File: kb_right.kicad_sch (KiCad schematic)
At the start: 175 parts, among them J1 10029449-001RLF, J2 Conn_01x03, J3 Conn_01x06, J4 Conn_01x08, J5 Conn_01x09, SW0 RotaryEncoder_Switch

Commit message: added 1.75u right shift
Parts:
- added D32: D_Small, Diode_SMD:D_SOD-123, symbol Device:D_Small
- added MX32: MX-NoLED, MX_Only:MXOnly-2.75U-Hotswap-ReversedStabilizers, symbol MX_Alps_Hybrid:MX-NoLED
- added MX32_1: MX-NoLED, MX_Only:MXOnly-1.75U-Hotswap, symbol MX_Alps_Hybrid:MX-NoLED
- MX32_2: renamed from MX32; footprint MX_Only:MXOnly-2.75U-Hotswap -> MX_Only:MXOnly-1U-Hotswap
- renumbered D32 to D32_1
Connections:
- net COL5: now also MX32.1 (COL), MX32_1.1 (COL)
- net COL6: now also J5.2 (Pin_2); no longer J5.1 (Pin_1)
- net COL7: now also J5.8 (Pin_8); no longer J5.7 (Pin_7)
- net COL8: now also J5.9 (Pin_9); no longer J5.8 (Pin_8)
- net GND: now also J5.1 (Pin_1); no longer J5.9 (Pin_9)
- net ROW5: now also J5.3 (Pin_3); no longer J5.2 (Pin_2)
- net ROW6: now also J5.4 (Pin_4); no longer J5.3 (Pin_3)
- net ROW7: now also J5.5 (Pin_5); no longer J5.4 (Pin_4)
- net ROW8: now also J5.6 (Pin_6), D32.1 (K); no longer J5.5 (Pin_5)
- net ROW9: now also J5.7 (Pin_7); no longer J5.6 (Pin_6)
- new net: D32.2 (A), MX32.2 (ROW), MX32_1.2 (ROW)

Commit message: fixed split right shift
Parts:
- MX32: footprint MX_Only:MXOnly-2.75U-Hotswap-ReversedStabilizers -> MX_Only:MXOnly-2.75U-Hotswap
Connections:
- net COL6: now also J5.1 (Pin_1); no longer J5.2 (Pin_2)
- net COL7: now also J5.7 (Pin_7); no longer J5.8 (Pin_8)
- net COL8: now also J5.8 (Pin_8); no longer J5.9 (Pin_9)
- net GND: now also J5.9 (Pin_9); no longer J5.1 (Pin_1)
- net ROW5: now also J5.2 (Pin_2); no longer J5.3 (Pin_3)
- net ROW6: now also J5.3 (Pin_3); no longer J5.4 (Pin_4)
- net ROW7: now also J5.4 (Pin_4); no longer J5.5 (Pin_5)
- net ROW8: now also J5.5 (Pin_5); no longer J5.6 (Pin_6)
- net ROW9: now also J5.6 (Pin_6); no longer J5.7 (Pin_7)
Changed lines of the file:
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@@
     (stroke (width 0) (type default) (color 0 0 0 0))
   )
-  (wire (pts (xy 375.92 130.81) (xy 384.81 130.81))
-    (stroke (width 0) (type default) (color 0 0 0 0))
-  )
   (wire (pts (xy 132.08 46.99) (xy 132.08 52.07))
     (stroke (width 0) (type default) (color 0 0 0 0))
@@
     (stroke (width 0) (type default) (color 0 0 0 0))
   )
+  (label "COL7" (at 384.81 146.05 180)
+    (effects (font (size 1.27 1.27)) (justify right bottom))
+  )
   (label "COL4" (at 180.34 24.13 90)
     (effects (font (size 1.27 1.27)) (justify left bottom))
   )
+  (label "ROW8" (at 384.81 140.97 180)
+    (effects (font (size 1.27 1.27)) (justify right bottom))
+  )
   (label "COL0" (at 396.24 31.75 0)
     (effects (font (size 1.27 1.27)) (justify left bottom))
   )
-  (label "ROW7" (at 384.81 140.97 180)
-    (effects (font (size 1.27 1.27)) (justify right bottom))
-  )
   (label "ROW8" (at 30.48 139.7 180)
     (effects (font (size 1.27 1.27)) (justify right bottom))
@@
     (effects (font (size 1.27 1.27)) (justify left bottom))
   )
+  (label "COL6" (at 384.81 130.81 180)
+    (effects (font (size 1.27 1.27)) (justify right bottom))
+  )
   (label "ROW9" (at 370.84 24.13 180)
     (effects (font (size 1.27 1.27)) (justify right bottom))
@@
     (effects (font (size 1.27 1.27)) (justify right bottom))
   )
-  (label "ROW8" (at 384.81 143.51 180)
-    (effects (font (size 1.27 1.27)) (justify right bottom))
-  )
   (label "RGB_IN" (at 370.84 46.99 180)
     (effects (font (size 1.27 1.27)) (justify right bottom))
@@
     (effects (font (size 1.27 1.27)) (justify left bottom))
   )
-  (label "ROW6" (at 384.81 138.43 180)
-    (effects (font (size 1.27 1.27)) (justify right bottom))
-  )
   (label "ROW7" (at 370.84 26.67 180)
     (effects (font (size 1.27 1.27)) (justify right bottom))
@@
     (effects (font (size 1.27 1.27)) (justify right bottom))
   )
-  (label "COL8" (at 384.81 151.13 180)
+  (label "ROW9" (at 384.81 143.51 180)
     (effects (font (size 1.27 1.27)) (justify right bottom))
   )
@@
     (effects (font (size 1.27 1.27)) (justify right bottom))
   )
-  (label "COL6" (at 384.81 133.35 180)
-    (effects (font (size 1.27 1.27)) (justify right bottom))
-  )
   (label "COL1" (at 97.79 24.13 90)
     (effects (font (size 1.27 1.27)) (justify left bottom))
@@
     (effects (font (size 1.27 1.27)) (justify right bottom))
   )
+  (label "ROW6" (at 384.81 135.89 180)
+    (effects (font (size 1.27 1.27)) (justify right bottom))
+  )
   (label "ENC_R1" (at 273.05 33.02 180)
     (effects (font (size 1.27 1.27)) (justify right bottom))
@@
     (effects (font (size 1.27 1.27)) (justify right bottom))
   )
-  (label "COL7" (at 384.81 148.59 180)
-    (effects (font (size 1.27 1.27)) (justify right bottom))
-  )
   (label "COL3" (at 370.84 34.29 180)
     (effects (font (size 1.27 1.27)) (justify right bottom))
@@
     (effects (font (size 1.27 1.27)) (justify right bottom))
   )
-  (label "ROW5" (at 384.81 135.89 180)
+  (label "COL8" (at 384.81 148.59 180)
     (effects (font (size 1.27 1.27)) (justify right bottom))
   )
@@
     (effects (font (size 1.27 1.27)) (justify left bottom))
   )
+  (label "ROW7" (at 384.81 138.43 180)
+    (effects (font (size 1.27 1.27)) (justify right bottom))
+  )
   (label "COL2" (at 396.24 34.29 0)
     (effects (font (size 1.27 1.27)) (justify left bottom))
@@
     (effects (font (size 1.27 1.27)) (justify left bottom))
   )
-  (label "ROW9" (at 384.81 146.05 180)
+  (label "ROW5" (at 384.81 133.35 180)
     (effects (font (size 1.27 1.27)) (justify right bottom))
   )
@@
     (pin "2")
   )
+  (symbol (lib_id "power:GND") (at 384.81 151.13 0) (unit 1)
+    (in_bom yes) (on_board yes) (fields_autoplaced)
+    (property "Reference" "#PWR?" (id 0) (at 384.81 157.48 0)
+      (effects (font (size 1.27 1.27)) hide)
+    )
+    (property "Value" "GND" (id 1) (at 384.81 156.21 0))
+    (property "Footprint" "" (id 2) (at 384.81 151.13 0)
+      (effects (font (size 1.27 1.27)) hide)
+    )
+    (property "Datasheet" "" (id 3) (at 384.81 151.13 0)
+      (effects (font (size 1.27 1.27)) hide)
+    )
+    (pin "1")
+  )
   (symbol (lib_id "power:GND") (at 255.27 262.89 0) (unit 1)
     (in_bom yes) (on_board yes) (fields_autoplaced)
@@
     (pin "2")
   )
-  (symbol (lib_id "power:GND") (at 375.92 130.81 0) (unit 1)
-    (in_bom yes) (on_board yes) (fields_autoplaced)
-    (property "Reference" "#PWR?" (id 0) (at 375.92 137.16 0)
-      (effects (font (size 1.27 1.27)) hide)
-    )
-    (property "Value" "GND" (id 1) (at 375.92 135.89 0))
-    (property "Footprint" "" (id 2) (at 375.92 130.81 0)
-      (effects (font (size 1.27 1.27)) hide)
-    )
-    (property "Datasheet" "" (id 3) (at 375.92 130.81 0)
-      (effects (font (size 1.27 1.27)) hide)
-    )
-    (pin "1")
-  )
   (symbol (lib_id "MX_Alps_Hybrid:MX-NoLED") (at 245.11 151.13 0) (unit 1)
     (in_bom yes) (on_board yes) (fields_autoplaced)
@@
       (effects (font (size 0.508 0.508)))
     )
-    (property "Footprint" "MX_Only:MXOnly-2.75U-Hotswap-ReversedStabilizers" (id 2) (at 182.245 122.555 0)
+    (property "Footprint" "MX_Only:MXOnly-2.75U-Hotswap" (id 2) (at 182.245 122.555 0)
       (effects (font (size 1.524 1.524)) hide)
     )
@@
       (reference "#PWR0187") (unit 1) (value "GND") (footprint "")
     )
-    (path "/7671b0de-2d92-498f-bb82-68e62219ea0b"
+    (path "/186d1e69-91a9-4165-a3fa-c15cfabc85a4"
       (reference "#PWR?") (unit 1) (value "GND") (footprint "")
     )
@@
     )
     (path "/bd5c7f90-342e-4ce2-8a8f-16d10e92a244"
-      (reference "MX32") (unit 1) (value "MX-NoLED") (footprint "MX_Only:MXOnly-2.75U-Hotswap-ReversedStabilizers")
+      (reference "MX32") (unit 1) (value "MX-NoLED") (footprint "MX_Only:MXOnly-2.75U-Hotswap")
     )
     (path "/b6c0f7f7-0224-4f0f-b9e7-b06cd4a6b8bd"

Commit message: start thru hole
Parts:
- added C?: 0.1uF, Capacitor_SMD:C_0805_2012Metric_Pad1.18x1.45mm_HandSolder, symbol Device:C_Small
- added D36: D_Small, Diode_SMD:D_SOD-123, symbol Device:D_Small
- added D?: SK6812MINI, Keebio-Parts:SK6812-MINI-E, symbol LED:WS2812B
- added MX36: MX-NoLED, MX_Only:MXOnly-1.25U-Hotswap, symbol MX_Alps_Hybrid:MX-NoLED
- added MX40_1: MX-NoLED, MX_Only:MXOnly-1.75U-Hotswap, symbol MX_Alps_Hybrid:MX-NoLED
- renumbered D36 to D37, D37 to D38, D38 to D39, D39 to D40, D40 to D41, D41 to D42, D42 to D43, MX36 to MX37, MX37 to MX38, MX38 to MX39, MX39 to MX40, MX40 to MX41, MX41 to MX42, MX42 to MX43
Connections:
- net +5V: now also C?.1, D?.1 (VDD)
- net COL0: now also J1.9; no longer J1.6
- net COL1: now also J1.8, MX36.1 (COL); no longer J1.7
- net COL2: now also J1.7; no longer J1.8
- net COL3: now also J1.6; no longer J1.9
- net COL4: now also J1.5; no longer J1.10
- net COL5: now also J1.4, MX40_1.1 (COL); no longer J1.11
- net COL6: now also J1.3; no longer J1.12
- net COL7: now also J1.2; no longer J1.13
- net COL8: now also J1.1; no longer J1.14
- net GND: now also C?.2, D?.3 (VSS)
- net ROW5: now also J1.10; no longer J1.5
- net ROW6: now also J1.11; no longer J1.4
- net ROW7: now also J1.12; no longer J1.3
- net ROW8: now also J1.13; no longer J1.2
- net ROW9: now also J1.14, D36.1 (K); no longer J1.1
- net at D142.2 (DOUT): now also D?.4 (DIN)
- net at D40.2 (A), MX40.2 (ROW): now also MX40_1.2 (ROW)
- new net: D36.2 (A), MX36.2 (ROW)

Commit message: try again - add rgb routing
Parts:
- removed C?: 0.1uF, Capacitor_SMD:C_0805_2012Metric_Pad1.18x1.45mm_HandSolder, symbol Device:C_Small
- removed D0, D43: D_Small, Diode_SMD:D_SOD-123, symbol Device:D_Small
- removed D?: SK6812MINI, Keebio-Parts:SK6812-MINI-E, symbol LED:WS2812B
- removed MX40_1: MX-NoLED, MX_Only:MXOnly-1.75U-Hotswap, symbol MX_Alps_Hybrid:MX-NoLED
- removed MX43: MX-NoLED, MX_Only:MXOnly-1U-Hotswap, symbol MX_Alps_Hybrid:MX-NoLED
- removed SW0: RotaryEncoder_Switch, Keebio-Parts:RotaryEncoder_EC11, symbol Device:RotaryEncoder_Switch
- added D45, D9: D_Small, Diode_SMD:D_SOD-123, symbol Device:D_Small
- added MX7_1: MX-NoLED, MX_Only:MXOnly-2U-Hotswap, symbol MX_Alps_Hybrid:MX-NoLED
- added MX9: MX-NoLED, MX_Only:MXOnly-1U-Hotswap, symbol MX_Alps_Hybrid:MX-NoLED
- added SW1: RotaryEncoder_Switch, Keebio-Parts:RotaryEncoder_EC11, symbol Device:RotaryEncoder_Switch
- MX41: renamed from MX40; footprint MX_Only:MXOnly-1.25U-Hotswap -> MX_Only:MXOnly-1U-Hotswap
- MX7: footprint MX_Only:MXOnly-2U-Hotswap -> MX_Only:MXOnly-1U-Hotswap
- renumbered D9 to D10, D10 to D11, D11 to D12, D12 to D13, D13 to D14, D14 to D15, D15 to D16, D16 to D17, D17 to D18, D18 to D19, D19 to D20, D20 to D21, D21 to D22, D22 to D23, D23 to D24, D24 to D25, D25 to D26, D26 to D27, D27 to D28, D28 to D29, D29 to D30, D30 to D31, D31 to D32, D32 to D35, D35 to D36, D36 to D37, D37 to D38, D38 to D39, D39 to D40, D40 to D41, D41 to D42, D42 to D43, MX9 to MX10, MX10 to MX11, MX11 to MX12, MX12 to MX13, MX13 to MX14, MX14 to MX15, MX15 to MX16, MX16 to MX17, MX17 to MX18, MX18 to MX19, MX19 to MX20, MX20 to MX21, MX21 to MX22, MX22 to MX23, MX23 to MX24, MX24 to MX25, MX25 to MX26, MX26 to MX27, MX27 to MX28, MX28 to MX29, MX29 to MX30, MX30 to MX31, MX31 to MX32, MX32_2 to MX32_1, MX32_1 to MX32_2, MX32 to MX33, MX33 to MX34, MX34 to MX35, MX35 to MX36, MX36 to MX37, MX37 to MX38, MX38 to MX39, MX39 to MX40, MX41 to MX42, MX42 to MX43
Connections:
- net COL6: now also MX7_1.1 (COL)
- net COL8: now also MX9.1 (COL), SW1.S1
- net ENC_R1: now also SW1.A
- net ENC_R2: now also SW1.B
- net GND: now also SW1.C
- net RGB_IN: now also D108.4 (DIN); no longer D101.4 (DIN)
- net ROW5: now also D9.1 (K)
- net ROW9: now also D45.1 (K)
- net at D106.2 (DOUT): now also D105.4 (DIN); no longer D107.4 (DIN)
- net at D106.4 (DIN): now also D107.2 (DOUT); no longer D105.2 (DOUT)
- net at D142.2 (DOUT): now also D141.4 (DIN)
- net at D142.4 (DIN): now also D134.2 (DOUT); no longer D141.2 (DOUT)
- net at D108.2 (DOUT): now also D107.4 (DIN); no longer D109.4 (DIN)
- net at D140.2 (DOUT): now also D139.4 (DIN); no longer D141.4 (DIN)
- net at D121.2 (DOUT): now also D120.4 (DIN); no longer D122.4 (DIN)
- net at D121.4 (DIN): now also D122.2 (DOUT); no longer D120.2 (DOUT)
- net at D104.2 (DOUT): now also D103.4 (DIN); no longer D105.4 (DIN)
- net at D104.4 (DIN): now also D105.2 (DOUT); no longer D103.2 (DOUT)
- net at D128.4 (DIN): now also D119.2 (DOUT); no longer D127.2 (DOUT)
- net at D7.2 (A), MX7.2 (ROW): now also MX7_1.2 (ROW)
- net at D127.4 (DIN): now also D118.2 (DOUT); no longer D126.2 (DOUT)
- net at D102.2 (DOUT): now also D101.4 (DIN); no longer D103.4 (DIN)
- net at D135.4 (DIN): now also D136.2 (DOUT); no longer D134.2 (DOUT)
- net at D123.4 (DIN): now also D124.2 (DOUT); no longer D122.2 (DOUT)
- net at D119.4 (DIN): now also D120.2 (DOUT); no longer D118.2 (DOUT)
- net at D123.2 (DOUT): now also D122.4 (DIN); no longer D124.4 (DIN)
- net at D126.4 (DIN): now also D127.2 (DOUT); no longer D125.2 (DOUT)
- net at D125.4 (DIN): now also D126.2 (DOUT); no longer D124.2 (DOUT)
- net at D140.4 (DIN): now also D141.2 (DOUT); no longer D139.2 (DOUT)
- net at D102.4 (DIN): now also D103.2 (DOUT); no longer D101.2 (DOUT)
- net at D138.2 (DOUT): now also D137.4 (DIN); no longer D139.4 (DIN)
- net at D138.4 (DIN): now also D139.2 (DOUT); no longer D137.2 (DOUT)
- net at D136.4 (DIN): now also D137.2 (DOUT); no longer D135.2 (DOUT)
- new net: D45.2 (A), SW1.S2
- new net: D101.2 (DOUT), D109.4 (DIN)
- new net: D124.4 (DIN), D125.2 (DOUT)
- new net: D9.2 (A), MX9.2 (ROW)
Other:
- moved on the sheet: C109, C110, C111, C112, C113, C114, C115, C116, C117, C118, C119, C120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

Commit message: most routing done
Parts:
- D1, D10, D11, D12, D13, D14, D15, D19, D2, D20, D21, D22, D23, D24, D28, D29, D3, D30, D31, D32, D36, D37, D38, D39, D4, D40, D41, D5, D6: footprint Diode_SMD:D_SOD-123 -> Keebio-Parts:Diode-Hybrid-Back
- D33: renamed from D35; footprint Diode_SMD:D_SOD-123 -> Keebio-Parts:Diode-Hybrid-Back
- renumbered D32_1 to D33_1, D33 to D34, D34 to D35, D45 to D44
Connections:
- net COL0: now also J1.1; no longer J1.9
- net COL1: now also J1.2; no longer J1.8
- net COL2: now also J1.3; no longer J1.7
- net COL3: now also J1.4; no longer J1.6
- net COL5: now also J1.6; no longer J1.4
- net COL6: now also J1.7; no longer J1.3
- net COL7: now also J1.8; no longer J1.2
- net COL8: now also J1.9; no longer J1.1
- net ENC_R1: now also J1.11; no longer J1.16
- net ENC_R2: now also J1.10; no longer J1.15
- net ROW5: now also J1.12; no longer J1.10
- net ROW6: now also J1.13; no longer J1.11
- net ROW7: now also J1.14; no longer J1.12
- net ROW8: now also J1.15; no longer J1.13
- net ROW9: now also J1.16; no longer J1.14
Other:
- moved on the sheet: D33, D7, MX32_2, MX33

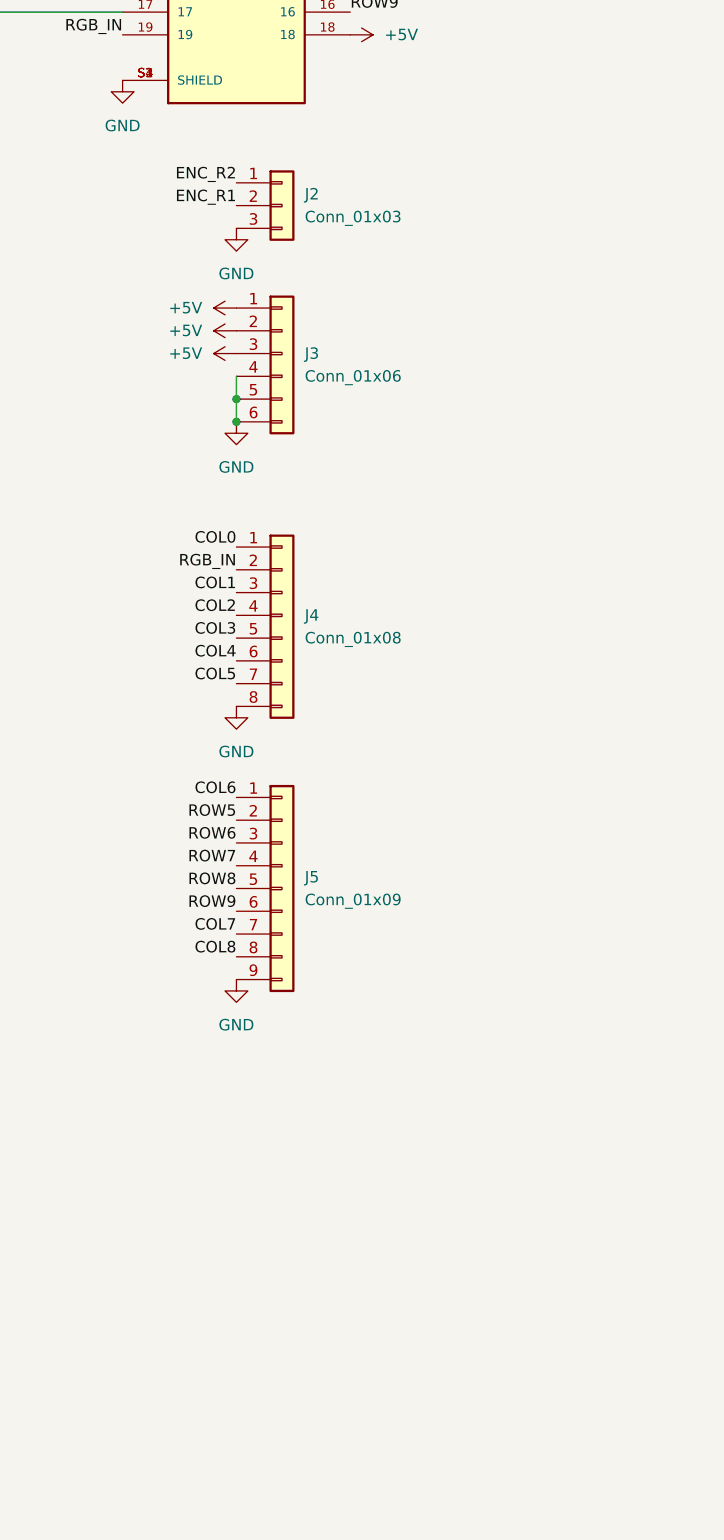
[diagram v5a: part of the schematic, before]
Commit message: routed test points
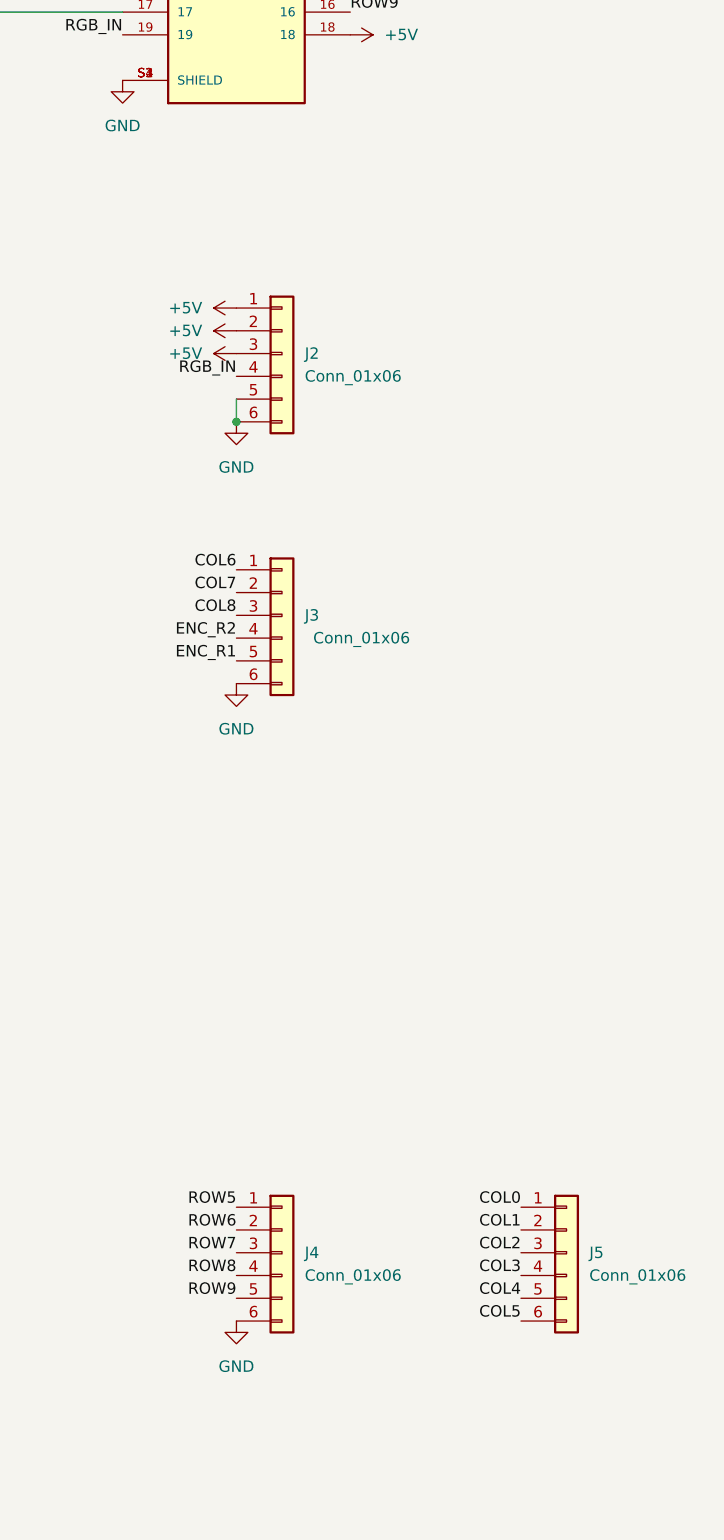
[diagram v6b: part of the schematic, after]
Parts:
- removed J2: Conn_01x03, Connector_PinHeader_2.54mm:PinHeader_1x03_P2.54mm_Vertical, symbol Connector_Generic:Conn_01x03
- removed J5: Conn_01x09, Connector_PinHeader_2.54mm:PinHeader_1x09_P2.54mm_Vertical, symbol Connector_Generic:Conn_01x09
- added J4, J5: Conn_01x06, Connector_PinHeader_2.54mm:PinHeader_1x06_P2.54mm_Vertical, symbol Connector_Generic:Conn_01x06
- J3: renamed from J4; value Conn_01x08 -> Conn_01x06; footprint Connector_PinHeader_2.54mm:PinHeader_1x08_P2.54mm_Vertical -> Connector_PinHeader_2.54mm:PinHeader_1x06_P2.54mm_Vertical; symbol Connector_Generic:Conn_01x08 -> Connector_Generic:Conn_01x06
- renumbered J3 to J2
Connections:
- net COL0: now also J5.1 (Pin_1); no longer J3.1 (Pin_1)
- net COL1: now also J5.2 (Pin_2); no longer J3.3 (Pin_3)
- net COL2: now also J5.3 (Pin_3); no longer J3.4 (Pin_4)
- net COL3: now also J5.4 (Pin_4); no longer J3.5 (Pin_5)
- net COL4: now also J5.5 (Pin_5); no longer J3.6 (Pin_6)
- net COL5: now also J5.6 (Pin_6); no longer J3.7 (Pin_7)
- net COL6: now also J3.1 (Pin_1)
- net COL7: now also J3.2 (Pin_2)
- net COL8: now also J3.3 (Pin_3)
- net ENC_R1: now also J3.5 (Pin_5)
- net ENC_R2: now also J3.4 (Pin_4)
- net GND: now also J3.6 (Pin_6), J4.6 (Pin_6); no longer J2.4 (Pin_4), J3.8 (Pin_8)
- net RGB_IN: now also J2.4 (Pin_4); no longer J3.2 (Pin_2)
- net ROW5: now also J4.1 (Pin_1)
- net ROW6: now also J4.2 (Pin_2)
- net ROW7: now also J4.3 (Pin_3)
- net ROW8: now also J4.4 (Pin_4)
- net ROW9: now also J4.5 (Pin_5)
